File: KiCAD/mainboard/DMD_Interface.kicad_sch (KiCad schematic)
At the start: 0 parts

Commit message: pain! dmd interface grind part 1
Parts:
- added C116, C122, C123, C124, C13, C137, C14, C15: 100n, Capacitor_SMD:C_0402_1005Metric, symbol Device:C
- added C117, C118, C119: 220n, Capacitor_SMD:C_0402_1005Metric, symbol Device:C
- added J1: AXT550124, tp_library:AXT550124, symbol tp_library:AXT550124
- added J30: Conn_01x08_Pin, Connector_PinHeader_2.54mm:PinHeader_1x08_P2.54mm_Vertical, symbol Connector:Conn_01x08_Pin
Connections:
- new net DMD_DEN_ARSTZ: J1.4
- new net DMD_HS_CLK_N: J1.14
- new net DMD_HS_CLK_P: J1.13
- new net DMD_HS_WDATAA_N: J1.19
- new net DMD_HS_WDATAA_P: J1.18
- new net DMD_HS_WDATAB_N: J1.17
- new net DMD_HS_WDATAB_P: J1.16
- new net DMD_HS_WDATAC_N: J1.32
- new net DMD_HS_WDATAC_P: J1.33
- new net DMD_HS_WDATAD_N: J1.34
- new net DMD_HS_WDATAD_P: J1.35
- new net DMD_HS_WDATAE_N: J1.40
- new net DMD_HS_WDATAE_P: J1.41
- new net DMD_HS_WDATAF_N: J1.42
- new net DMD_HS_WDATAF_P: J1.43
- new net DMD_HS_WDATAG_N: J1.11
- new net DMD_HS_WDATAG_P: J1.10 (19)
- new net DMD_HS_WDATAH_N: J1.9
- new net DMD_HS_WDATAH_P: J1.8
- new net DMD_LS_CLK: J1.6
- new net DMD_LS_RDATA: J1.3
- new net DMD_LS_WDATA: J1.5
- new net GND: C116.2, C117.2, C118.2, C119.2, C122.2, C123.2, C124.2, C13.2, C137.2, C14.2, C15.2, J1.12, J1.15, J1.2, J1.20, J1.21, J1.22, J1.25 (49), J1.26, J1.30, J1.31, J1.36, J1.39, J1.44, J1.48, J1.49, J1.51 (MP1), J1.52 (MP2), J1.53 (MP3), J1.54 (MP4), J1.7
- new net P1P8V_DLPC: C116.1, C117.1, C118.1, C119.1, C137.1, J1.1, J1.37, J1.38, J1.50
- new net VBIAS: C123.1, C14.1, J1.46
- new net VOFS: C122.1, C15.1, J1.47
- new net VRST: C124.1, C13.1, J1.45
- no-connect marks 0 -> 5

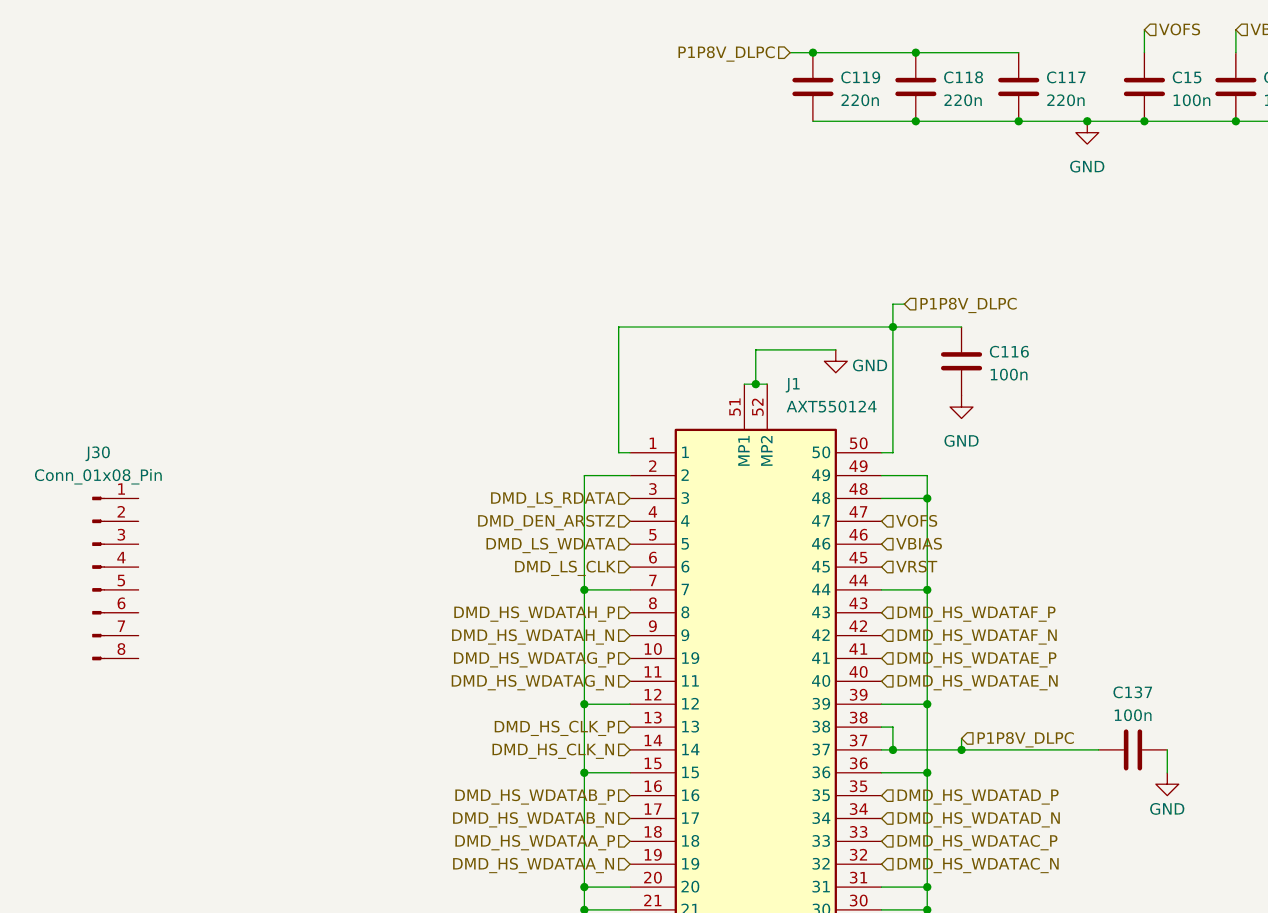
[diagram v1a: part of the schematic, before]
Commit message: spi connections to dlpc
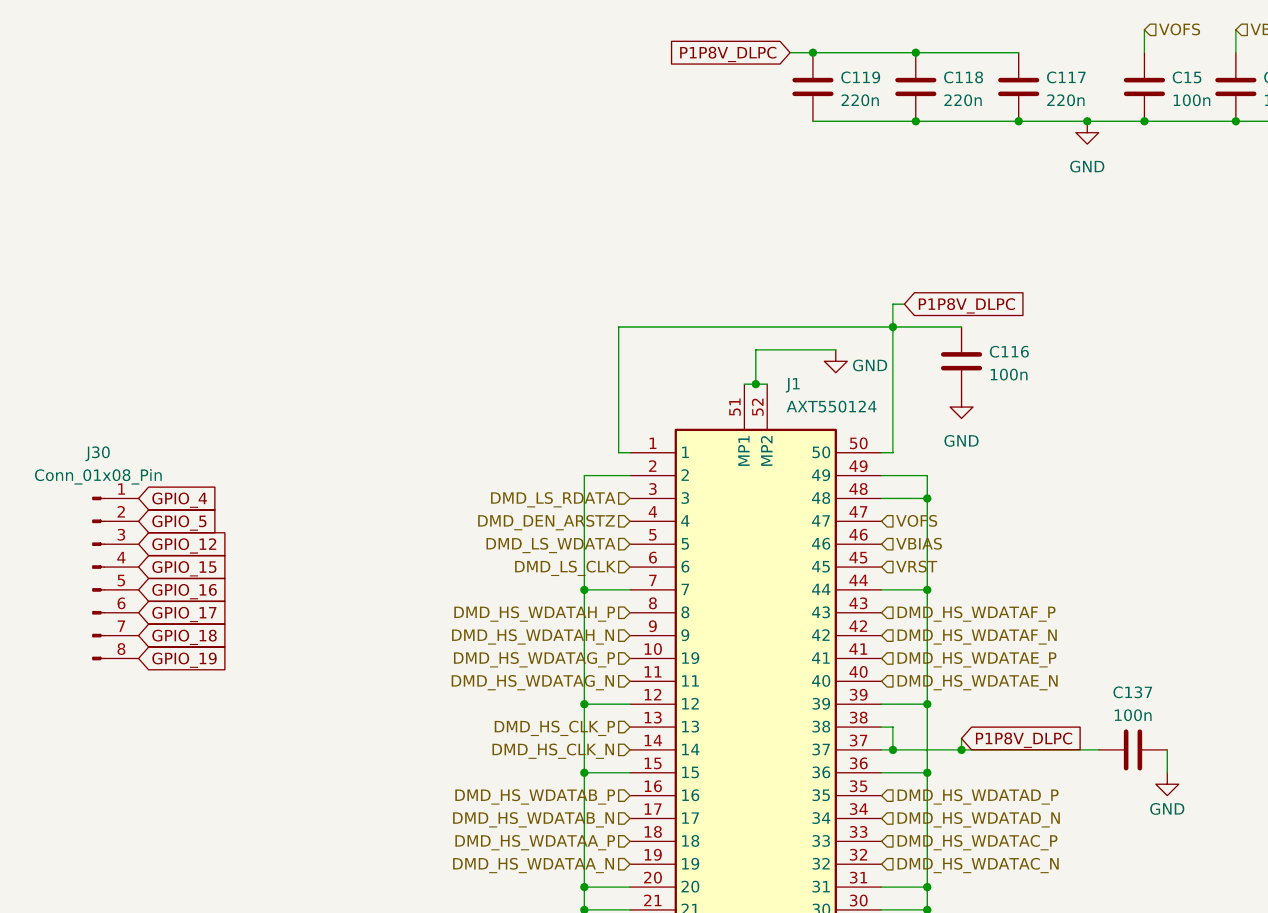
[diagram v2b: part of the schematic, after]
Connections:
- net GPIO_4: now reaches J30.1 (Pin_1)
- net GPIO_5: now reaches J30.2 (Pin_2)
- net GPIO_12: now reaches J30.3 (Pin_3)
- net GPIO_15: now reaches J30.4 (Pin_4)
- net GPIO_16: now reaches J30.5 (Pin_5)
- net GPIO_17: now reaches J30.6 (Pin_6)
- net GPIO_18: now reaches J30.7 (Pin_7)
- net GPIO_19: now reaches J30.8 (Pin_8)
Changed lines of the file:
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@@
+		)
+	)
+	(global_label "GPIO_5"
+		(shape input)
+		(at 115.57 77.47 0)
+		(fields_autoplaced yes)
+		(effects
+			(font
+				(size 1.27 1.27)
+			)
+			(justify left)
+		)
+		(property "Intersheetrefs" "${INTERSHEET_REFS}"
+			(at 125.2076 77.47 0)
+			(effects
+				(font
+					(size 1.27 1.27)
+				)
+				(justify left)
+				(hide yes)
+			)
+		)
+	)
+	(global_label "GPIO_18"
+		(shape input)
+		(at 115.57 90.17 0)
+		(fields_autoplaced yes)
+		(effects
+			(font
+				(size 1.27 1.27)
+			)
+			(justify left)
+		)
+		(property "Intersheetrefs" "${INTERSHEET_REFS}"
+			(at 126.4171 90.17 0)
+			(effects
+				(font
+					(size 1.27 1.27)
+				)
+				(justify left)
+				(hide yes)
+			)
+		)
+	)
+	(global_label "GPIO_19"
+		(shape input)
+		(at 115.57 92.71 0)
+		(fields_autoplaced yes)
+		(effects
+			(font
+				(size 1.27 1.27)
+			)
+			(justify left)
+		)
+		(property "Intersheetrefs" "${INTERSHEET_REFS}"
+			(at 126.4171 92.71 0)
+			(effects
+				(font
+					(size 1.27 1.27)
+				)
+				(justify left)
+				(hide yes)
+			)
+		)
+	)
+	(global_label "GPIO_15"
+		(shape input)
+		(at 115.57 82.55 0)
+		(fields_autoplaced yes)
+		(effects
+			(font
+				(size 1.27 1.27)
+			)
+			(justify left)
+		)
+		(property "Intersheetrefs" "${INTERSHEET_REFS}"
+			(at 126.4171 82.55 0)
+			(effects
+				(font
+					(size 1.27 1.27)
+				)
+				(justify left)
+				(hide yes)
+			)
+		)
+	)
+	(global_label "GPIO_12"
+		(shape input)
+		(at 115.57 80.01 0)
+		(fields_autoplaced yes)
+		(effects
+			(font
+				(size 1.27 1.27)
+			)
+			(justify left)
+		)
+		(property "Intersheetrefs" "${INTERSHEET_REFS}"
+			(at 126.4171 80.01 0)
+			(effects
+				(font
+					(size 1.27 1.27)
+				)
+				(justify left)
+				(hide yes)
+			)
+		)
+	)
+	(global_label "GPIO_16"
+		(shape input)
+		(at 115.57 85.09 0)
+		(fields_autoplaced yes)
+		(effects
+			(font
+				(size 1.27 1.27)
+			)
+			(justify left)
+		)
+		(property "Intersheetrefs" "${INTERSHEET_REFS}"
+			(at 126.4171 85.09 0)
+			(effects
+				(font
+					(size 1.27 1.27)
+				)
+				(justify left)
+				(hide yes)
+			)
+		)
+	)
+	(global_label "GPIO_17"
+		(shape input)
+		(at 115.57 87.63 0)
+		(fields_autoplaced yes)
+		(effects
+			(font
+				(size 1.27 1.27)
+			)
+			(justify left)
+		)
+		(property "Intersheetrefs" "${INTERSHEET_REFS}"
+			(at 126.4171 87.63 0)
+			(effects
+				(font
+					(size 1.27 1.27)
+				)
+				(justify left)
+				(hide yes)
+			)
+		)
+	)
+	(global_label "P1P8V_DLPC"
+		(shape input)
+		(at 187.96 25.4 180)
+		(fields_autoplaced yes)
+		(effects
+			(font
+				(size 1.27 1.27)
+			)
+			(justify right)
+		)
+		(property "Intersheetrefs" "${INTERSHEET_REFS}"
+			(at 173.1215 25.4 0)
+			(effects
+				(font
+					(size 1.27 1.27)
+				)
+				(justify right)
+				(hide yes)
+			)
+		)
+	)
+	(global_label "GPIO_4"
+		(shape input)
+		(at 115.57 74.93 0)
+		(fields_autoplaced yes)
+		(effects
+			(font
+				(size 1.27 1.27)
+			)
+			(justify left)
+		)
+		(property "Intersheetrefs" "${INTERSHEET_REFS}"
+			(at 125.2076 74.93 0)
+			(effects
+				(font
+					(size 1.27 1.27)
+				)
+				(justify left)
+				(hide yes)
+			)
+		)
+	)
+	(global_label "P1P8V_DLPC"
+		(shape input)
+		(at 207.01 101.6 0)
+		(fields_autoplaced yes)
+		(effects
+			(font
+				(size 1.27 1.27)
+			)
+			(justify left)
+		)
+		(property "Intersheetrefs" "${INTERSHEET_REFS}"
+			(at 221.8485 101.6 0)
+			(effects
+				(font
+					(size 1.27 1.27)
+				)
+				(justify left)
+				(hide yes)
+			)
+		)
+	)
+	(global_label "P1P8V_DLPC"
+		(shape input)
+		(at 200.66 53.34 0)
+		(fields_autoplaced yes)
+		(effects
+			(font
+				(size 1.27 1.27)
+			)
+			(justify left)
+		)
+		(property "Intersheetrefs" "${INTERSHEET_REFS}"
+			(at 215.4985 53.34 0)
+			(effects
+				(font
+					(size 1.27 1.27)
+				)
+				(justify left)
+				(hide yes)
+			)
 		)
 	)
@@
 		)
 	)
-	(hierarchical_label "P1P8V_DLPC"
-		(shape input)
-		(at 187.96 25.4 180)
-		(effects
-			(font
-				(size 1.27 1.27)
-			)
-			(justify right)
-		)
-	)
 	(hierarchical_label "DMD_HS_WDATAB_N"
 		(shape input)
@@
 		)
 	)
-	(hierarchical_label "P1P8V_DLPC"
-		(shape input)
-		(at 207.01 101.6 0)
-		(effects
-			(font
-				(size 1.27 1.27)
-			)
-			(justify left)
-		)
-	)
 	(hierarchical_label "DMD_HS_WDATAC_P"
 		(shape input)
@@
 		(effects
 			(font
-				(size 1.27 1.27)
-			)
-			(justify left)
-		)
-	)
-	(hierarchical_label "P1P8V_DLPC"
-		(shape input)
-		(at 200.66 53.34 0)
-		(effects
-			(font

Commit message: dmd interface done!
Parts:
- added D6: LED, LED_SMD:LED_1206_3216Metric, symbol Device:LED
- added IC3: SN74AUP1G06DCKR, tp_library:SOT65P210X110-5N, symbol tp_library:SN74AUP1G06DCKR
- added IC4, IC5: SN74AUP1G07DCKR, tp_library:SOT65P210X110-5N, symbol tp_library:SN74AUP1G07DCKR
- added J10: Conn_01x05_Pin, Connector_PinHeader_2.54mm:PinHeader_1x05_P2.54mm_Vertical, symbol Connector:Conn_01x05_Pin
- added R15, R197: 10k, Resistor_SMD:R_0402_1005Metric, symbol Device:R_US
- added R6: 150, Resistor_SMD:R_0402_1005Metric, symbol Device:R_US
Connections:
- net GND: now also IC3.3 (GND), IC4.3 (GND), IC5.3 (GND), J10.1 (Pin_1)
- net P1P8V_DLPC: now also IC3.5 (VCC), IC4.5 (VCC), IC5.5 (VCC)
- new net GPIO_6: IC3.2 (A), IC4.2 (A)
- new net GPIO_9: IC5.2 (A)
- new net P3V3V: D6.2 (A), R15.1, R197.1
- new net PRINT_ACTIVE: IC5.4 (Y), R197.2
- new net SPI1_CLK: J10.5 (Pin_5)
- new net SPI1_CSZ0: J10.4 (Pin_4)
- new net SPI1_MISO: J10.2 (Pin_2)
- new net SPI1_MOSI: J10.3 (Pin_3)
- new net SYS_RDY: IC4.4 (Y), R15.2
- new net SYS_RDY_LED: D6.1 (K), R6.1
- new net SYS_RDY_LED_DRV: IC3.4 (Y), R6.2
- no-connect marks 5 -> 8
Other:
- moved on the sheet: C116, C117, C118, C119, C122, C123, C124, C13, C137, C14, C15, J1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

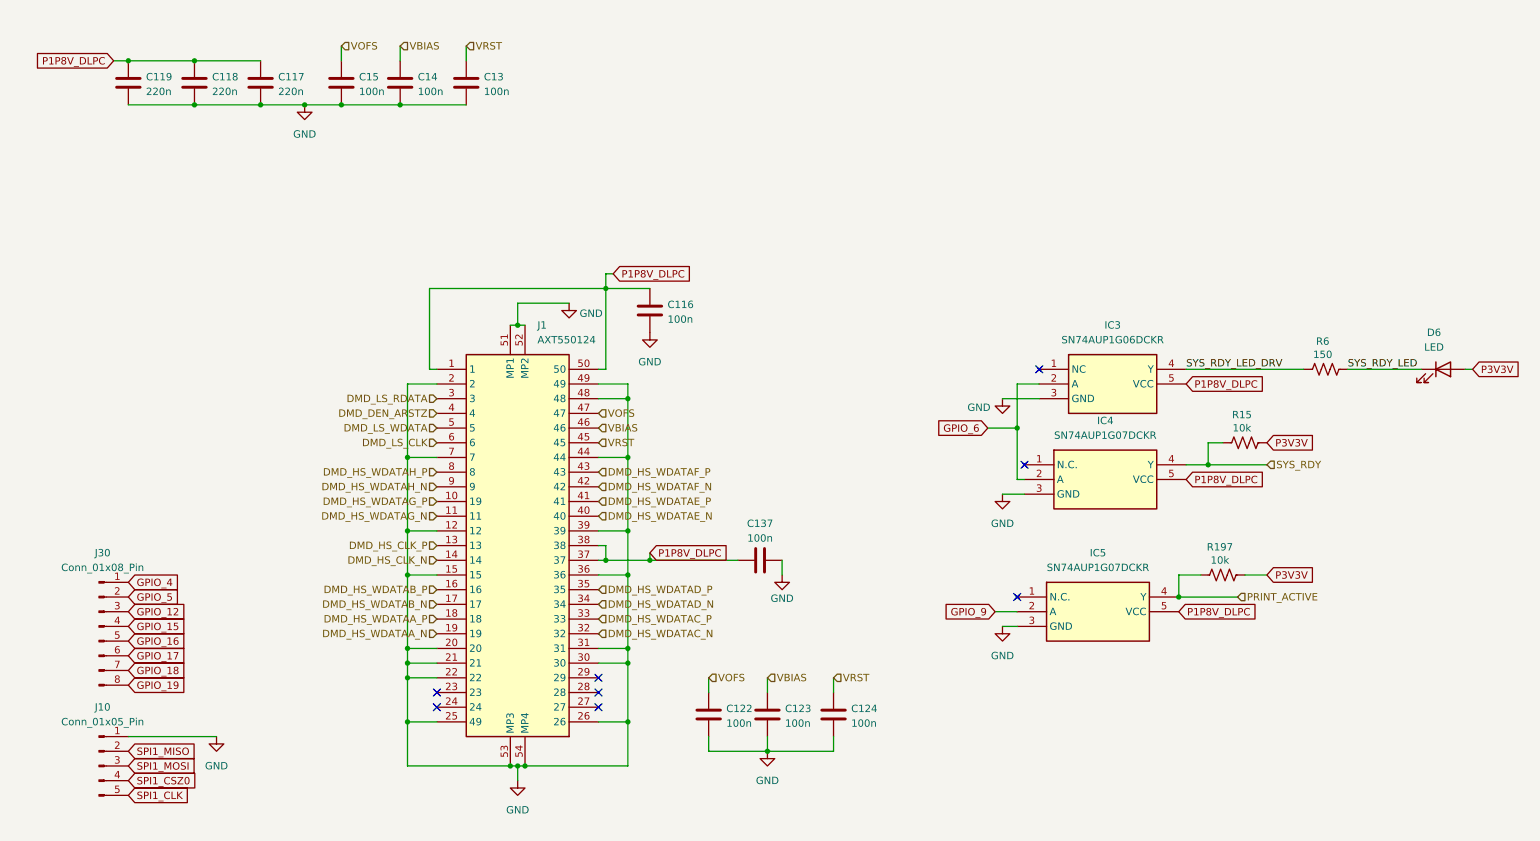
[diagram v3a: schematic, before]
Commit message: humanly readable now
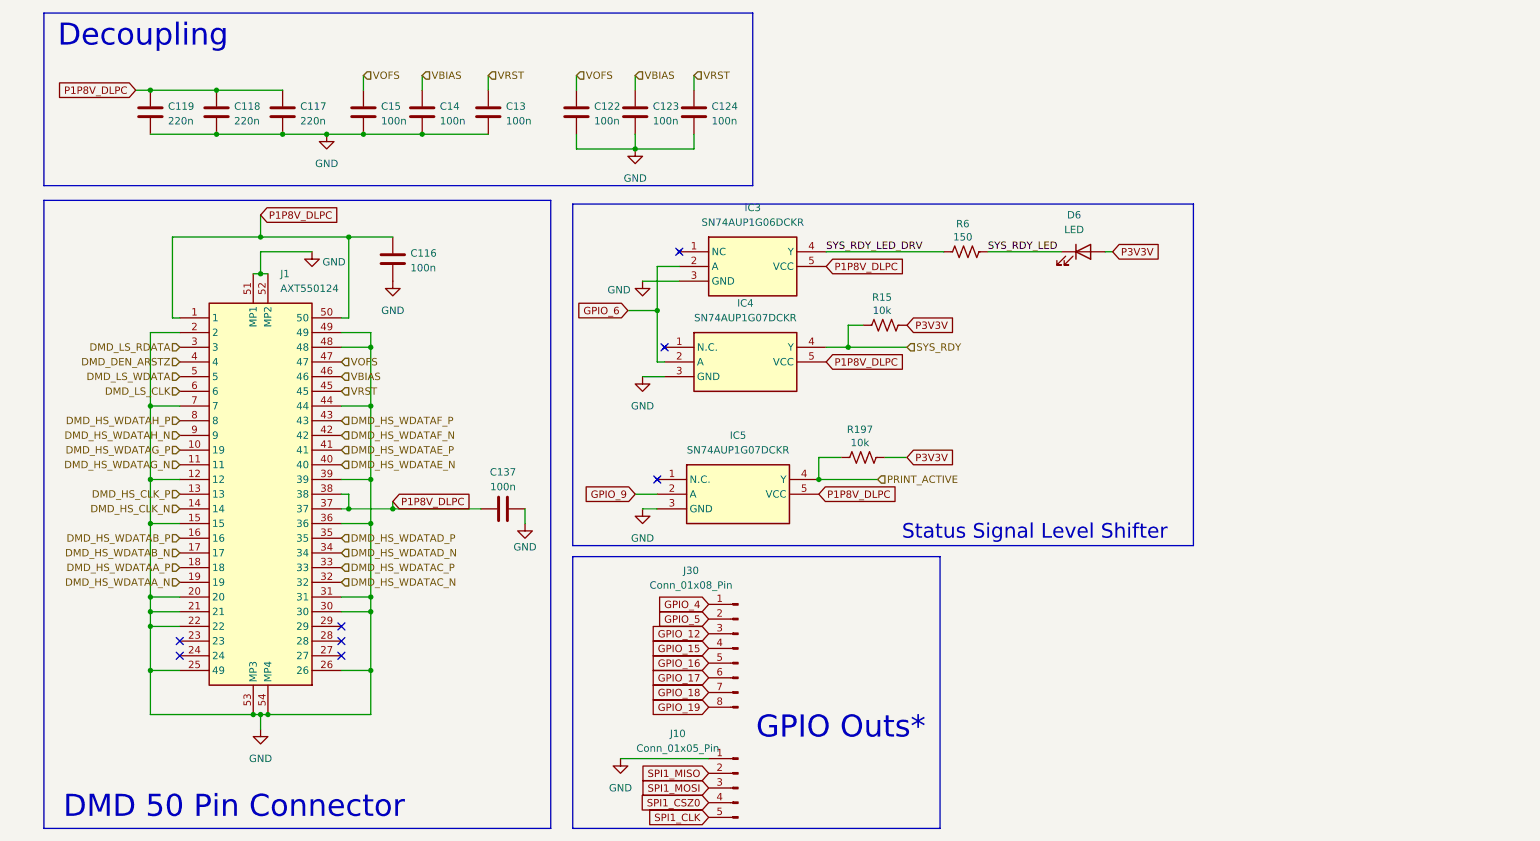
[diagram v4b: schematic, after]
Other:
- note added: "DMD 50 Pin Connector"
- note added: "Decoupling"
- note added: "GPIO Outs*"
- note added: "Status Signal Level Shifter"
- moved on the sheet: C116, C117, C118, C119, C122, C123, C124, C13, C137, C14, C15, D6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
